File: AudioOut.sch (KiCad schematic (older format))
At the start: 8 parts, among them J12 Audio-Jack-2, U9 TSH22IDT

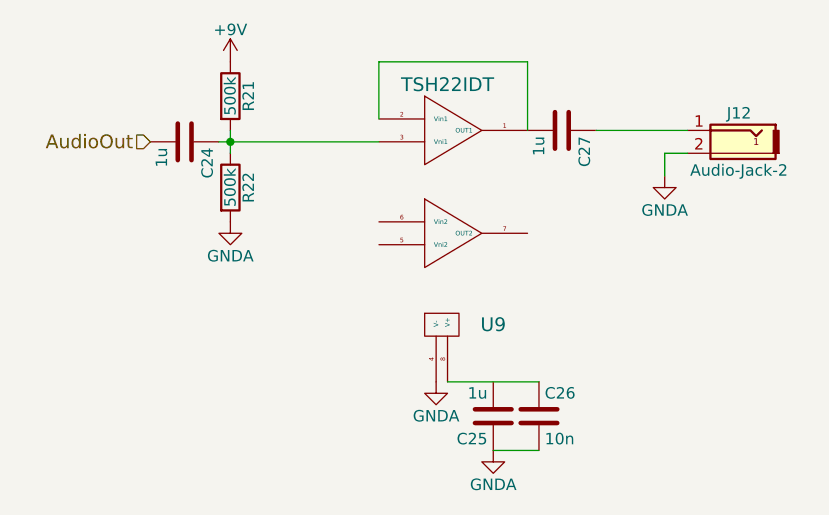
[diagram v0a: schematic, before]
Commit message: Halfway through layout. Started libraries.
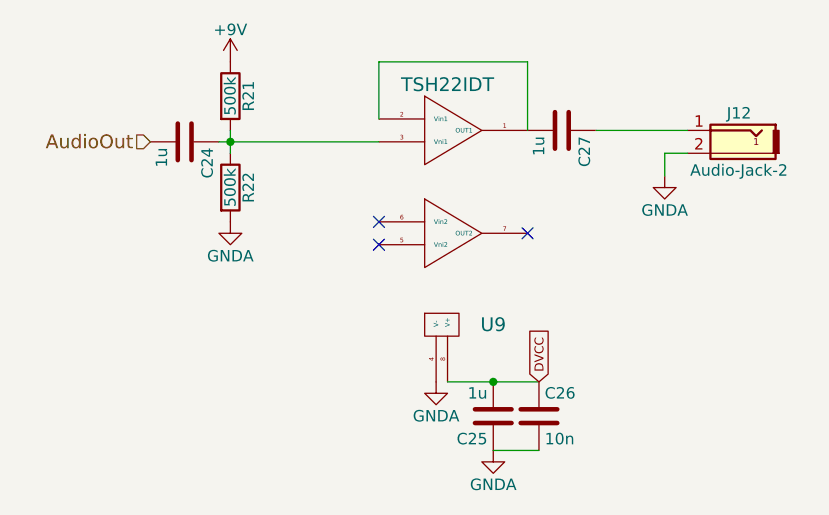
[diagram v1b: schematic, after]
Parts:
- J12: footprint (none) -> Modulin:SN37A14B
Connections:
- net DVCC: now reaches C26.1, U9.8 (V+)
- net DVCC: now also C25.2
- no-connect marks 0 -> 3
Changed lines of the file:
@@
 EESchema Schematic File Version 2
-LIBS:MyLib
+LIBS:74xgxx
+LIBS:74xx
 LIBS:ac-dc
+LIBS:actel
 LIBS:adc-dac
+LIBS:allegro
 LIBS:Altera
 LIBS:analog_devices
@@
 LIBS:atmel
 LIBS:audio
-LIBS:Battery_Management
+LIBS:battery_management
 LIBS:bbd
 LIBS:bosch
 LIBS:brooktre
-LIBS:Connector
+LIBS:cmos_ieee
+LIBS:cmos4000
+LIBS:conn
 LIBS:contrib
 LIBS:cypress
@@
 LIBS:device
 LIBS:digital-audio
-LIBS:Diode
-LIBS:Display
-LIBS:driver_gate
+LIBS:diode
+LIBS:display
 LIBS:dsp
-LIBS:DSP_Microchip_DSPIC33
 LIBS:elec-unifil
 LIBS:ESD_Protection
-LIBS:Espressif
-LIBS:FPGA_Actel
 LIBS:ftdi
 LIBS:gennum
-LIBS:Graphic
+LIBS:graphic_symbols
 LIBS:hc11
 LIBS:infineon
@@
 LIBS:ir
 LIBS:Lattice
-LIBS:LED
+LIBS:leds
 LIBS:LEM
 LIBS:linear
-LIBS:Logic_74xgxx
-LIBS:Logic_74xx
-LIBS:Logic_CMOS_4000
-LIBS:Logic_CMOS_IEEE
 LIBS:logic_programmable
-LIBS:Logic_TTL_IEEE
 LIBS:maxim
-LIBS:MCU_Microchip_PIC10
-LIBS:MCU_Microchip_PIC12
-LIBS:MCU_Microchip_PIC16
-LIBS:MCU_Microchip_PIC18
-LIBS:MCU_Microchip_PIC24
-LIBS:MCU_Microchip_PIC32
-LIBS:MCU_NXP_Kinetis
-LIBS:MCU_NXP_LPC
-LIBS:MCU_NXP_S08
-LIBS:MCU_ST_STM8
-LIBS:MCU_ST_STM32
-LIBS:MCU_Texas_MSP430
-LIBS:Mechanical
+LIBS:mechanical
 LIBS:memory
 LIBS:microchip
+LIBS:microchip_dspic33dsc
+LIBS:microchip_pic10mcu
+LIBS:microchip_pic12mcu
+LIBS:microchip_pic16mcu
+LIBS:microchip_pic18mcu
+LIBS:microchip_pic24mcu
+LIBS:microchip_pic32mcu
 LIBS:microcontrollers
 LIBS:modules
-LIBS:Motor
 LIBS:motor_drivers
 LIBS:motorola
+LIBS:motors
+LIBS:msp430
 LIBS:nordicsemi
 LIBS:nxp
+LIBS:nxp_armmcu
 LIBS:onsemi
 LIBS:opto
@@
 LIBS:references
 LIBS:regul
-LIBS:Relay
+LIBS:relays
 LIBS:rfcom
 LIBS:RFSolutions
-LIBS:Sensor_Current
 LIBS:sensors
 LIBS:silabs
 LIBS:siliconi
+LIBS:stm8
+LIBS:stm32
 LIBS:supertex
-LIBS:Switch
+LIBS:switches
 LIBS:texas
-LIBS:Transformer
-LIBS:Transistor
+LIBS:transf
+LIBS:transistors
 LIBS:triac_thyristor
-LIBS:Valve
+LIBS:ttl_ieee
+LIBS:valves
 LIBS:video
 LIBS:wiznet
@@
 LIBS:zetex
 LIBS:Zilog
-LIBS:74xgxx
-LIBS:74xx
-LIBS:actel
-LIBS:cmos_ieee
-LIBS:cmos4000
-LIBS:conn
-LIBS:logo
-LIBS:microchip_dspic33dsc
-LIBS:microchip_pic10mcu
-LIBS:microchip_pic12mcu
-LIBS:microchip_pic16mcu
-LIBS:microchip_pic18mcu
-LIBS:microchip_pic32mcu
-LIBS:msp430
-LIBS:nxp_armmcu
-LIBS:relays
-LIBS:stm8
-LIBS:stm32
-LIBS:switches
-LIBS:transf
-LIBS:transistors
-LIBS:ttl_ieee
-LIBS:valves
+LIBS:MyLib
 LIBS:Modulin-cache
 EELAYER 25 0
@@
 $EndComp
 $Comp
-L GNDA #PWR041
+L GNDA #PWR048
 U 1 1 5A165618
 P 4350 3200
-F 0 "#PWR041" H 4350 2950 50  0001 C CNN
+F 0 "#PWR048" H 4350 2950 50  0001 C CNN
 F 1 "GNDA" H 4350 3050 50  0000 C CNN
 F 2 "" H 4350 3200 50  0001 C CNN
@@
 $EndComp
 $Comp
-L +9V #PWR042
+L +9V #PWR049
 U 1 1 5A1656C9
 P 4350 2500
-F 0 "#PWR042" H 4350 2350 50  0001 C CNN
+F 0 "#PWR049" H 4350 2350 50  0001 C CNN
 F 1 "+9V" H 4350 2640 50  0000 C CNN
 F 2 "" H 4350 2500 50  0001 C CNN
@@
 $EndComp
 $Comp
-L GNDA #PWR043
+L GNDA #PWR050
 U 1 1 5A1659C9
 P 5500 4200
-F 0 "#PWR043" H 5500 3950 50  0001 C CNN
+F 0 "#PWR050" H 5500 3950 50  0001 C CNN
 F 1 "GNDA" H 5500 4050 50  0000 C CNN
 F 2 "" H 5500 4200 50  0001 C CNN
@@
 	5650 2500 5650 2800
 Wire Wire Line
+	5700 4200 5500 4200
+Wire Wire Line
 	5300 3900 5700 3900
-Wire Wire Line
-	5700 4200 5500 4200
-Wire Wire Line
-	5500 3900 5500 3900
-$Comp
-L GNDA #PWR044
+$Comp
+L GNDA #PWR051
 U 1 1 5A165AFD
 P 5250 3900
-F 0 "#PWR044" H 5250 3650 50  0001 C CNN
+F 0 "#PWR051" H 5250 3650 50  0001 C CNN
 F 1 "GNDA" H 5250 3750 50  0000 C CNN
 F 2 "" H 5250 3900 50  0001 C CNN
@@
 F 0 "J12" H 6525 2875 50  0000 C CNN
 F 1 "Audio-Jack-2" H 6525 2625 50  0000 C CNN
-F 2 "" H 6800 2800 50  0001 C CNN
+F 2 "Modulin:SN37A14B" H 6800 2800 50  0001 C CNN
 F 3 "" H 6800 2800 50  0001 C CNN
 	1    6550 2800
@@
 $EndComp
 $Comp
-L GNDA #PWR045
+L GNDA #PWR052
 U 1 1 5A165D53
 P 6250 3000
-F 0 "#PWR045" H 6250 2750 50  0001 C CNN
+F 0 "#PWR052" H 6250 2750 50  0001 C CNN
 F 1 "GNDA" H 6250 2850 50  0000 C CNN
 F 2 "" H 6250 3000 50  0001 C CNN
@@
 Text HLabel 4000 2850 0    60   Input ~ 0
 AudioOut
+NoConn ~ 5650 3250
+NoConn ~ 5000 3200
+NoConn ~ 5000 3300
+Text GLabel 5700 3900 1    39   Input ~ 0
+DVCC
+Connection ~ 5500 3900
 $EndSCHEMATC

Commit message: Finished board Rev 1
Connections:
- net GNDA renamed GNDD
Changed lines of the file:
@@
 EESchema Schematic File Version 2
-LIBS:74xgxx
-LIBS:74xx
+LIBS:Modulin-rescue
 LIBS:ac-dc
-LIBS:actel
 LIBS:adc-dac
-LIBS:allegro
 LIBS:Altera
 LIBS:analog_devices
@@
 LIBS:atmel
 LIBS:audio
-LIBS:battery_management
+LIBS:Battery_Management
 LIBS:bbd
 LIBS:bosch
 LIBS:brooktre
-LIBS:cmos_ieee
-LIBS:cmos4000
-LIBS:conn
+LIBS:Connector
 LIBS:contrib
 LIBS:cypress
@@
 LIBS:device
 LIBS:digital-audio
-LIBS:diode
-LIBS:display
+LIBS:Diode
+LIBS:Display
+LIBS:driver_gate
 LIBS:dsp
+LIBS:DSP_Microchip_DSPIC33
 LIBS:elec-unifil
 LIBS:ESD_Protection
+LIBS:Espressif
+LIBS:FPGA_Actel
 LIBS:ftdi
 LIBS:gennum
-LIBS:graphic_symbols
+LIBS:Graphic
 LIBS:hc11
 LIBS:infineon
@@
 LIBS:ir
 LIBS:Lattice
-LIBS:leds
+LIBS:LED
 LIBS:LEM
 LIBS:linear
+LIBS:Logic_74xgxx
+LIBS:Logic_74xx
+LIBS:Logic_CMOS_4000
+LIBS:Logic_CMOS_IEEE
 LIBS:logic_programmable
+LIBS:Logic_TTL_IEEE
 LIBS:maxim
-LIBS:mechanical
+LIBS:MCU_Microchip_PIC10
+LIBS:MCU_Microchip_PIC12
+LIBS:MCU_Microchip_PIC16
+LIBS:MCU_Microchip_PIC18
+LIBS:MCU_Microchip_PIC24
+LIBS:MCU_Microchip_PIC32
+LIBS:MCU_NXP_Kinetis
+LIBS:MCU_NXP_LPC
+LIBS:MCU_NXP_S08
+LIBS:MCU_ST_STM8
+LIBS:MCU_ST_STM32
+LIBS:MCU_Texas_MSP430
+LIBS:Mechanical
 LIBS:memory
 LIBS:microchip
-LIBS:microchip_dspic33dsc
-LIBS:microchip_pic10mcu
-LIBS:microchip_pic12mcu
-LIBS:microchip_pic16mcu
-LIBS:microchip_pic18mcu
-LIBS:microchip_pic24mcu
-LIBS:microchip_pic32mcu
 LIBS:microcontrollers
 LIBS:modules
+LIBS:Motor
 LIBS:motor_drivers
 LIBS:motorola
-LIBS:motors
-LIBS:msp430
 LIBS:nordicsemi
 LIBS:nxp
-LIBS:nxp_armmcu
 LIBS:onsemi
 LIBS:opto
@@
 LIBS:references
 LIBS:regul
-LIBS:relays
+LIBS:Relay
 LIBS:rfcom
 LIBS:RFSolutions
+LIBS:Sensor_Current
 LIBS:sensors
 LIBS:silabs
 LIBS:siliconi
-LIBS:stm8
-LIBS:stm32
 LIBS:supertex
-LIBS:switches
+LIBS:Switch
 LIBS:texas
-LIBS:transf
-LIBS:transistors
+LIBS:Transformer
+LIBS:Transistor
 LIBS:triac_thyristor
-LIBS:ttl_ieee
-LIBS:valves
+LIBS:Valve
 LIBS:video
 LIBS:wiznet
@@
 LIBS:zetex
 LIBS:Zilog
+LIBS:74xgxx
+LIBS:74xx
+LIBS:actel
+LIBS:cmos_ieee
+LIBS:cmos4000
+LIBS:conn
+LIBS:microchip_dspic33dsc
+LIBS:microchip_pic10mcu
+LIBS:microchip_pic12mcu
+LIBS:microchip_pic16mcu
+LIBS:microchip_pic18mcu
+LIBS:microchip_pic32mcu
+LIBS:msp430
+LIBS:nxp_armmcu
+LIBS:relays
+LIBS:stm8
+LIBS:stm32
+LIBS:switches
+LIBS:transf
+LIBS:transistors
+LIBS:ttl_ieee
+LIBS:valves
 LIBS:MyLib
 LIBS:Modulin-cache
@@
 $EndComp
 $Comp
-L GNDA #PWR048
-U 1 1 5A165618
-P 4350 3200
-F 0 "#PWR048" H 4350 2950 50  0001 C CNN
-F 1 "GNDA" H 4350 3050 50  0000 C CNN
-F 2 "" H 4350 3200 50  0001 C CNN
-F 3 "" H 4350 3200 50  0001 C CNN
-	1    4350 3200
-	1    0    0    -1
-$EndComp
-$Comp
 L +9V #PWR049
 U 1 1 5A1656C9
@@
 	1    0    0    -1
 $EndComp
-$Comp
-L GNDA #PWR050
-U 1 1 5A1659C9
-P 5500 4200
-F 0 "#PWR050" H 5500 3950 50  0001 C CNN
-F 1 "GNDA" H 5500 4050 50  0000 C CNN
-F 2 "" H 5500 4200 50  0001 C CNN
-F 3 "" H 5500 4200 50  0001 C CNN
-	1    5500 4200
-	1    0    0    -1
-$EndComp
 Wire Wire Line
 	4300 2850 5000 2850
@@
 	5650 2500 5650 2800
 Wire Wire Line
-	5700 4200 5500 4200
+	5250 4200 5700 4200
 Wire Wire Line
 	5300 3900 5700 3900
-$Comp
-L GNDA #PWR051
-U 1 1 5A165AFD
-P 5250 3900
-F 0 "#PWR051" H 5250 3650 50  0001 C CNN
-F 1 "GNDA" H 5250 3750 50  0000 C CNN
-F 2 "" H 5250 3900 50  0001 C CNN
-F 3 "" H 5250 3900 50  0001 C CNN
-	1    5250 3900
-	1    0    0    -1
-$EndComp
 $Comp
 L Audio-Jack-2 J12
@@
 	-1   0    0    -1
 $EndComp
-$Comp
-L GNDA #PWR052
-U 1 1 5A165D53
-P 6250 3000
-F 0 "#PWR052" H 6250 2750 50  0001 C CNN
-F 1 "GNDA" H 6250 2850 50  0000 C CNN
-F 2 "" H 6250 3000 50  0001 C CNN
-F 3 "" H 6250 3000 50  0001 C CNN
-	1    6250 3000
-	1    0    0    -1
-$EndComp
 Wire Wire Line
 	6250 3000 6250 2900
@@
 DVCC
 Connection ~ 5500 3900
+$Comp
+L GNDD #PWR?
+U 1 1 5A1B3C22
+P 5500 4200
+F 0 "#PWR?" H 5500 3950 50  0001 C CNN
+F 1 "GNDD" H 5500 4075 50  0000 C CNN
+F 2 "" H 5500 4200 50  0001 C CNN
+F 3 "" H 5500 4200 50  0001 C CNN
+	1    5500 4200
+	1    0    0    -1
+$EndComp
+Wire Wire Line
+	5250 3900 5250 4200
+Connection ~ 5500 4200
+$Comp
+L GNDD #PWR?
+U 1 1 5A1B3D6B
+P 4350 3200
+F 0 "#PWR?" H 4350 2950 50  0001 C CNN
+F 1 "GNDD" H 4350 3075 50  0000 C CNN
+F 2 "" H 4350 3200 50  0001 C CNN
+F 3 "" H 4350 3200 50  0001 C CNN
+	1    4350 3200
+	1    0    0    -1
+$EndComp
+$Comp
+L GNDD #PWR?
+U 1 1 5A1B3DC0
+P 6250 3000
+F 0 "#PWR?" H 6250 2750 50  0001 C CNN
+F 1 "GNDD" H 6250 2875 50  0000 C CNN
+F 2 "" H 6250 3000 50  0001 C CNN
+F 3 "" H 6250 3000 50  0001 C CNN
+	1    6250 3000
+	1    0    0    -1
+$EndComp
 $EndSCHEMATC
